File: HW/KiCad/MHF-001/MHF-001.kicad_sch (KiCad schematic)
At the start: 137 parts, among them J1 DE15_Socket_HighDensity_Mount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, J10 I2C, J11 POWER, J12 Reset, J13 AREF, J14 XTAL2, J15 XTAL1, J16 AVCC, J2 Mini-DIN-6, J3 Conn_Coaxial, J4 Conn_02x32_Odd_Even, J5 USB_B_Micro, J6 02x32, J7 SPI, J8 AVR-ISP-6, J9 Serial, M3 CY7C109D-10ZXI, M5 CY7C109D-10ZXI, Q1 BC107, U1 ATMEGA2560-16AU, U10 74HC245, U11 74HC245, U12 74HC245, U13 CH340G, U14 AMS1117-5.0, U15 AMS1117-3.3, U2 74HC14, U3 74LS08, U4 74HC165, U6 74AHC373PW, U7 74HC595, U8 74HC595, U9 74HC157, Y1 16 MHz, Y2 12 MHz

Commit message: added some connectors
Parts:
- added J17: SDcard, Connector_PinHeader_2.54mm:PinHeader_1x06_P2.54mm_Vertical, symbol Connector_Generic:Conn_01x06
- added J18: RTC1, Connector_PinHeader_2.54mm:PinHeader_1x04_P2.54mm_Vertical, symbol Connector_Generic:Conn_01x04
- added J19: RTC2, Connector_PinHeader_2.54mm:PinHeader_1x06_P2.54mm_Vertical, symbol Connector_Generic:Conn_01x06
- added J20: SDcardpins, Connector_PinHeader_2.54mm:PinHeader_1x04_P2.54mm_Vertical, symbol Connector_Generic:Conn_01x04
- added J21: 5V, Connector_PinHeader_2.54mm:PinHeader_1x02_P2.54mm_Vertical, symbol Connector_Generic:Conn_02x01
- added J22: 3.3V, Connector_PinHeader_2.54mm:PinHeader_1x02_P2.54mm_Vertical, symbol Connector_Generic:Conn_02x01
- added J23: VIN 12V, Connector_BarrelJack:BarrelJack_Horizontal, symbol Connector:Barrel_Jack_Switch
- added JP1, JP2, JP3, JP4: SolderJumper_2_Bridged, Jumper:SolderJumper-2_P1.3mm_Bridged_Pad1.0x1.5mm, symbol Jumper:SolderJumper_2_Bridged
- J11: value POWER -> 5V
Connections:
- net +3.3V: now also J22.1 (Pin_1)
- net +5V: now also J10.2 (Pin_2), J11.1 (Pin_1), J11.3 (Pin_3), J11.5 (Pin_5), J7.5 (Pin_5), J17.5 (Pin_5), J18.2 (Pin_2), J19.2 (Pin_2), J21.1 (Pin_1); no longer J10.3 (Pin_3), J7.6 (Pin_6)
- net B16: now also JP92.3 (B)
- net GND: now also J10.1 (Pin_1), J7.6 (Pin_6), J17.6 (Pin_6), J18.1 (Pin_1), J19.1 (Pin_1), J21.2 (Pin_2), J22.2 (Pin_2), J23.2, J23.3; no longer J10.4 (Pin_4), J7.5 (Pin_5)
- net MISO: now also J7.4 (Pin_4), JP1.2 (B); no longer J7.1 (Pin_1)
- net MOSI: now also J7.3 (Pin_3), JP2.2 (B); no longer J7.2 (Pin_2)
- net SCK: now also J7.2 (Pin_2), JP3.2 (B); no longer J7.3 (Pin_3)
- net SCL: now also J10.4 (Pin_4), J18.4 (Pin_4), J19.4 (Pin_4); no longer J10.1 (Pin_1)
- net SDA: now also J10.3 (Pin_3), J18.3 (Pin_3), J19.3 (Pin_3); no longer J10.2 (Pin_2)
- net SS: now also J7.1 (Pin_1), JP4.2 (B); no longer J7.4 (Pin_4)
- net VIN: now also J23.1; no longer J11.1 (Pin_1), J11.3 (Pin_3), J11.5 (Pin_5)
- new net: J17.3 (Pin_3), J20.3 (Pin_3), JP2.1 (A)
- new net: J17.4 (Pin_4), J20.4 (Pin_4), JP1.1 (A)
- new net: J17.1 (Pin_1), J20.1 (Pin_1), JP4.1 (A)
- new net: J17.2 (Pin_2), J20.2 (Pin_2), JP3.1 (A)
- no-connect marks 50 -> 52
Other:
- moved on the sheet: F1, J5, R24, R25

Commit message: Final placement of parts (I hope)
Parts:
- removed J13: AREF, Connector_Wire:SolderWire-0.5sqmm_1x01_D0.9mm_OD2.1mm, symbol Connector_Generic:Conn_01x01
- removed J14: XTAL2, Connector_Wire:SolderWire-0.5sqmm_1x01_D0.9mm_OD2.1mm, symbol Connector_Generic:Conn_01x01
- removed J15: XTAL1, Connector_Wire:SolderWire-0.5sqmm_1x01_D0.9mm_OD2.1mm, symbol Connector_Generic:Conn_01x01
- removed J16: AVCC, Connector_Wire:SolderWire-0.5sqmm_1x01_D0.9mm_OD2.1mm, symbol Connector_Generic:Conn_01x01
- removed J18: RTC1, Connector_PinHeader_2.54mm:PinHeader_1x04_P2.54mm_Vertical, symbol Connector_Generic:Conn_01x04
- removed J19: RTC2, Connector_PinHeader_2.54mm:PinHeader_1x06_P2.54mm_Vertical, symbol Connector_Generic:Conn_01x06
- removed J21: 5V, Connector_PinHeader_2.54mm:PinHeader_1x02_P2.54mm_Vertical, symbol Connector_Generic:Conn_02x01
- removed J22: 3.3V, Connector_PinHeader_2.54mm:PinHeader_1x02_P2.54mm_Vertical, symbol Connector_Generic:Conn_02x01
- removed JP89, JP90, JP93: SolderJumper_2_Bridged, Jumper:SolderJumper-2_P1.3mm_Bridged_Pad1.0x1.5mm, symbol Jumper:SolderJumper_2_Bridged
- removed N4: ~, Gilhad:NetJoint, symbol PCM_Gilhad_symbols:NetJoint
- added J24: AND_B1, Connector_Wire:SolderWire-0.5sqmm_1x01_D0.9mm_OD2.1mm, symbol Connector_Generic:Conn_01x01
- added J25: AND_B2, Connector_Wire:SolderWire-0.5sqmm_1x01_D0.9mm_OD2.1mm, symbol Connector_Generic:Conn_01x01
- added J26: AND_C1, Connector_Wire:SolderWire-0.5sqmm_1x01_D0.9mm_OD2.1mm, symbol Connector_Generic:Conn_01x01
- added J27: AND_C2, Connector_Wire:SolderWire-0.5sqmm_1x01_D0.9mm_OD2.1mm, symbol Connector_Generic:Conn_01x01
- added J28: AND_D1, Connector_Wire:SolderWire-0.5sqmm_1x01_D0.9mm_OD2.1mm, symbol Connector_Generic:Conn_01x01
- added J29: AND_D2, Connector_Wire:SolderWire-0.5sqmm_1x01_D0.9mm_OD2.1mm, symbol Connector_Generic:Conn_01x01
- added J30: AND_Dx, Connector_Wire:SolderWire-0.5sqmm_1x01_D0.9mm_OD2.1mm, symbol Connector_Generic:Conn_01x01
- added J31: AND_Cx, Connector_Wire:SolderWire-0.5sqmm_1x01_D0.9mm_OD2.1mm, symbol Connector_Generic:Conn_01x01
- added J32: AND_Bx, Connector_Wire:SolderWire-0.5sqmm_1x01_D0.9mm_OD2.1mm, symbol Connector_Generic:Conn_01x01
- added J33: NOTF, Connector_Wire:SolderWire-0.5sqmm_1x01_D0.9mm_OD2.1mm, symbol Connector_Generic:Conn_01x01
- added J34: NOTE, Connector_Wire:SolderWire-0.5sqmm_1x01_D0.9mm_OD2.1mm, symbol Connector_Generic:Conn_01x01
- added J35: NOTEx, Connector_Wire:SolderWire-0.5sqmm_1x01_D0.9mm_OD2.1mm, symbol Connector_Generic:Conn_01x01
- added J36: NOTFx, Connector_Wire:SolderWire-0.5sqmm_1x01_D0.9mm_OD2.1mm, symbol Connector_Generic:Conn_01x01
- added JP10: ANDD2+, Jumper:SolderJumper-2_P1.3mm_Bridged_Pad1.0x1.5mm, symbol Jumper:SolderJumper_2_Bridged
- added JP11: NOTF, Jumper:SolderJumper-2_P1.3mm_Bridged_Pad1.0x1.5mm, symbol Jumper:SolderJumper_2_Bridged
- added JP12: NOTE, Jumper:SolderJumper-2_P1.3mm_Bridged_Pad1.0x1.5mm, symbol Jumper:SolderJumper_2_Bridged
- added JP5: ANDB1+, Jumper:SolderJumper-2_P1.3mm_Bridged_Pad1.0x1.5mm, symbol Jumper:SolderJumper_2_Bridged
- added JP6: ANDB2+, Jumper:SolderJumper-2_P1.3mm_Bridged_Pad1.0x1.5mm, symbol Jumper:SolderJumper_2_Bridged
- added JP7: ANDC1+, Jumper:SolderJumper-2_P1.3mm_Bridged_Pad1.0x1.5mm, symbol Jumper:SolderJumper_2_Bridged
- added JP8: ANDC2+, Jumper:SolderJumper-2_P1.3mm_Bridged_Pad1.0x1.5mm, symbol Jumper:SolderJumper_2_Bridged
- added JP9: ANDD1+, Jumper:SolderJumper-2_P1.3mm_Bridged_Pad1.0x1.5mm, symbol Jumper:SolderJumper_2_Bridged
- added N1: ~, NetTie:NetTie-2_SMD_Pad0.5mm, symbol Device:NetTie_2
- C1: value 100 pF?? -> 100 pF
- J1: value DE15_Socket_HighDensity_MountingHoles -> VGA
- J11: value 5V -> + 5V -; footprint Connector_PinHeader_2.54mm:PinHeader_2x03_P2.54mm_Vertical -> Connector_PinSocket_2.54mm:PinSocket_2x03_P2.54mm_Vertical
- J2: value Mini-DIN-6 -> PS/2
- J3: value Conn_Coaxial -> RCA; footprint other.pretty:CUI_RCJ-047 -> Gilhad:CUI_RCJ-047_Yellow
- J4: value Conn_02x32_Odd_Even -> SysBus
- J5: value USB_B_Micro -> Micro
- J6: value 02x32 -> SysBus
- J8: value AVR-ISP-6 -> ISP
- JP1: value SolderJumper_2_Bridged -> MISO
- JP100: value SolderJumper_3_Open -> SHRequest
- JP102: value SolderJumper_3_Open -> S_Enable
- JP103: value SolderJumper_3_Open -> S_Read
- JP104: value SolderJumper_3_Open -> S_Write
- JP105: value SolderJumper_3_Open -> GDdir
- JP106: value SolderJumper_3_Open -> GEnable
- JP107: value SolderJumper_3_Open -> GADir
- JP2: value SolderJumper_2_Bridged -> MOSI
- JP3: value SolderJumper_2_Bridged -> SCK
- JP4: value SolderJumper_2_Bridged -> SS
- JP55: value SolderJumper_2_Bridged -> PS2_Data; footprint Jumper:SolderJumper-2_P1.3mm_Bridged_Pad1.0x1.5mm -> Jumper:SolderJumper-2_P1.3mm_Open_RoundedPad1.0x1.5mm; symbol Jumper:SolderJumper_2_Bridged -> Jumper:SolderJumper_2_Open
- JP56: value SolderJumper_2_Bridged -> PS2_CLK; footprint Jumper:SolderJumper-2_P1.3mm_Bridged_Pad1.0x1.5mm -> Jumper:SolderJumper-2_P1.3mm_Open_RoundedPad1.0x1.5mm; symbol Jumper:SolderJumper_2_Bridged -> Jumper:SolderJumper_2_Open
- JP91: value SolderJumper_2_Bridged -> Inside
- JP92: value SolderJumper_3_Open -> X16
- JP94: value SolderJumper_3_Open -> A_HALT
- JP95: value SolderJumper_3_Open -> A_READ
- JP98: value SolderJumper_3_Open -> SHDirty
- JP99: value SolderJumper_3_Open -> SHGranted
- LED1: value LED -> RX
- LED2: value LED -> TX
- LED3: value LED -> ON
- LED4: value LED -> CTS
- LED5: value LED -> RTS
- LED6: value LED -> SCL
- N3: footprint Gilhad:NetJoint -> NetTie:NetTie-2_SMD_Pad0.5mm; symbol PCM_Gilhad_symbols:NetJoint -> Device:NetTie_2
- PA1: value Conn_01x08 -> PA
- PB1: value Conn_01x08 -> PB
- PC1: value Conn_01x08 -> PC
- PD1: value Conn_01x08 -> PD
- PE1: value Conn_01x08 -> PE
- PF1: value Conn_01x08 -> PF
- PG1: value Conn_01x06 -> PG
- PH1: value Conn_01x08 -> PH
- PJ1: value Conn_01x08 -> PJ
- PK1: value Conn_01x08 -> PK
- PL1: value Conn_01x08 -> PL
- R1: value 3k3 -> 3k3/22k
- R32, R33: value --- -> 4k7; now fitted
- S1: value TS06-667-30-BK-100-G-SMT-TR -> Reset
- U1: value ATMEGA2560-16AU -> ATMEGA2560
- U6: value 74AHC373PW -> 74AHC373
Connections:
- net Data is gone; now on net PS2 Data: J2.1, R12.1, U7.14 (SER)
- net +5V: now also U1.100 (AVCC), JP10.1 (A), JP11.1 (A), JP12.1 (A), JP5.1 (A), JP6.1 (A), JP7.1 (A), JP8.1 (A), JP9.1 (A)
- net GND: no longer U2.13, U3.12, U3.13
- net PS2 Clock: now also D1.1 (K), R1.2, U2.4, U7.12 (RCLK), U8.12 (RCLK)
- net SYNC_RCA: now also N1.1
- net VGA data 3: now also N3.2; no longer N3.1
- net VGA data 4: now also N1.2
- net ~{SUPRESS}: now also N3.1; no longer N3.2
- net at U3.6: now also J32.1 (Pin_1)
- net at U2.10: now also J35.1 (Pin_1)
- net at U2.12: now also J36.1 (Pin_1); no longer U2.11
- net Clock: no longer names the net of J2.5, R13.1, U2.1
- new net: J27.1 (Pin_1), JP8.2 (B), U3.10
- new net: J31.1 (Pin_1), U3.8
- new net: J26.1 (Pin_1), JP7.2 (B), U3.9
- new net: J24.1 (Pin_1), JP5.2 (B), U3.4
- new net: J25.1 (Pin_1), JP6.2 (B), U3.5
- new net: J33.1 (Pin_1), JP11.2 (B), U2.13
- new net: J28.1 (Pin_1), JP9.2 (B), U3.12
- new net: J29.1 (Pin_1), JP10.2 (B), U3.13
- new net: J30.1 (Pin_1), U3.11
- new net: J34.1 (Pin_1), JP12.2 (B), U2.11
- no-connect marks 52 -> 48
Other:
- note added: "Clock"
- note added: "Data"
- moved on the sheet: U2E, U2F, U3B, U3D

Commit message: WayWayWay and other final touches
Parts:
- added J13: +5V, Connector_Wire:SolderWire-0.5sqmm_1x01_D0.9mm_OD2.1mm, symbol Connector_Generic:Conn_01x01
- added J14: GND, Connector_Wire:SolderWire-0.5sqmm_1x01_D0.9mm_OD2.1mm, symbol Connector_Generic:Conn_01x01
- added JP13: Xhalt, Jumper:SolderJumper-2_P1.3mm_Bridged_Pad1.0x1.5mm, symbol Jumper:SolderJumper_2_Bridged
- added LED7: SPI, LED_SMD:LED_0805_2012Metric, symbol Device:LED
- added LED8: HALT, LED_SMD:LED_0805_2012Metric, symbol Device:LED
- added R41, R43: 1k, Resistor_SMD:R_0805_2012Metric_Pad1.20x1.40mm_HandSolder, symbol Device:R
- added R42: 1k, Resistor_SMD:R_0603_1608Metric_Pad0.98x0.95mm_HandSolder, symbol Device:R
- JP12: value NOTE -> HaltLED
- PA1: value PA -> PA0
- PB1: value PB -> PB0
- PC1: value PC -> PC0
- PD1: value PD -> PD0
- PE1: value PE -> PE0
- PF1: value PF -> PF0
- PG1: value PG -> PG0
- PH1: value PH -> PH0
- PJ1: value PJ -> PJ0
- PK1: value PK -> PK0
- PL1: value PL -> PL0
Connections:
- net +5V: now also J13.1 (Pin_1), R42.1; no longer JP12.1 (A)
- net GND: now also J14.1 (Pin_1), LED7.1 (K), LED8.1 (K)
- net SCK: now also R41.2
- net X_HALT: now also JP13.2 (B), R42.2; no longer PE1.6 (Pin_6), U1.7 ((OC3C/INT5)PE5)
- net at J35.1 (Pin_1), U2.10: now also R43.2
- new net: LED8.2 (A), R43.1
- new net: JP12.1 (A), JP13.1 (A), PE1.6 (Pin_6), U1.7 ((OC3C/INT5)PE5)
- new net: LED7.2 (A), R41.1
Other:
- moved on the sheet: C12, D2, J12, R26, S1, U2E

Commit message: condensators
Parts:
- added Cx1, Cx10, Cx11, Cx12, Cx13, Cx2, Cx3, Cx4, Cx5, Cx6, Cx7, Cx8, Cx9: Cx, Capacitor_THT:C_Disc_D3.0mm_W2.0mm_P2.50mm, symbol Device:C
- added Cx14, Cx15: Cx, Capacitor_THT:CP_Radial_D5.0mm_P2.50mm, symbol Device:C_Polarized
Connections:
- net +5V: now also Cx1.1, Cx10.1, Cx11.1, Cx12.1, Cx13.1, Cx14.1, Cx15.1, Cx2.1, Cx3.1, Cx4.1, Cx5.1, Cx6.1, Cx7.1, Cx8.1, Cx9.1
- net GND: now also Cx1.2, Cx10.2, Cx11.2, Cx12.2, Cx13.2, Cx14.2, Cx15.2, Cx2.2, Cx3.2, Cx4.2, Cx5.2, Cx6.2, Cx7.2, Cx8.2, Cx9.2

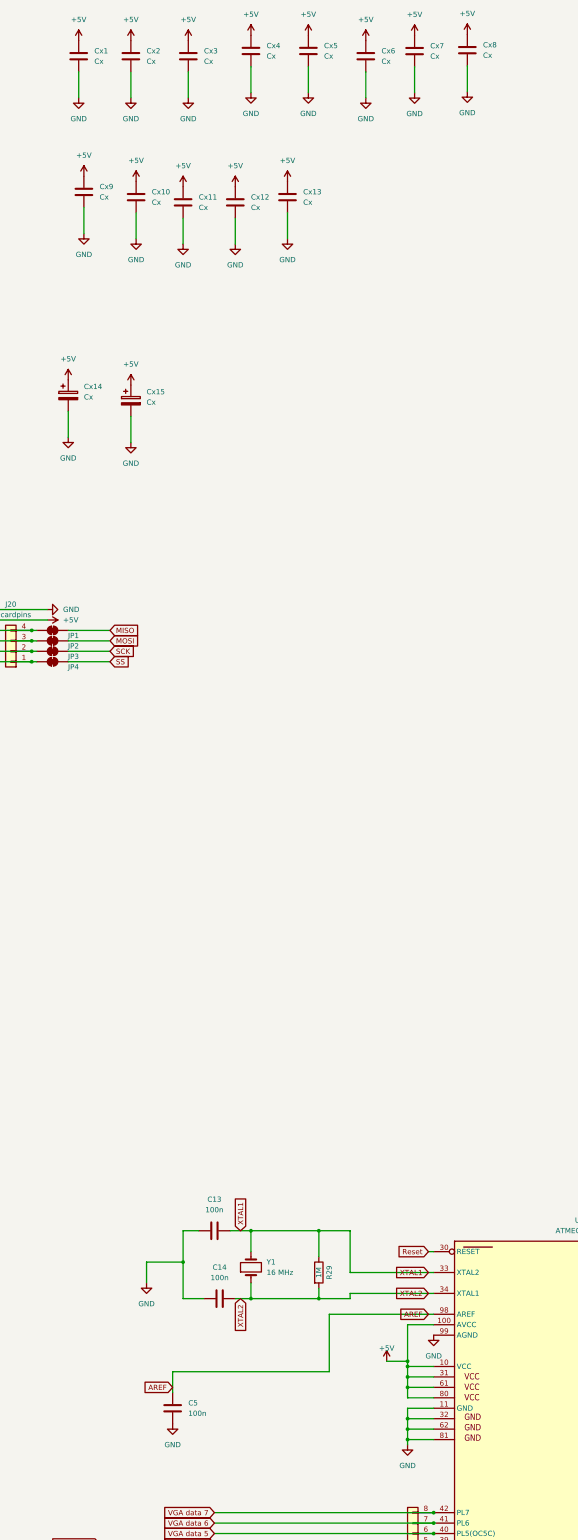
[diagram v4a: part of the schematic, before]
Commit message: XTALs, AVCC, AREF
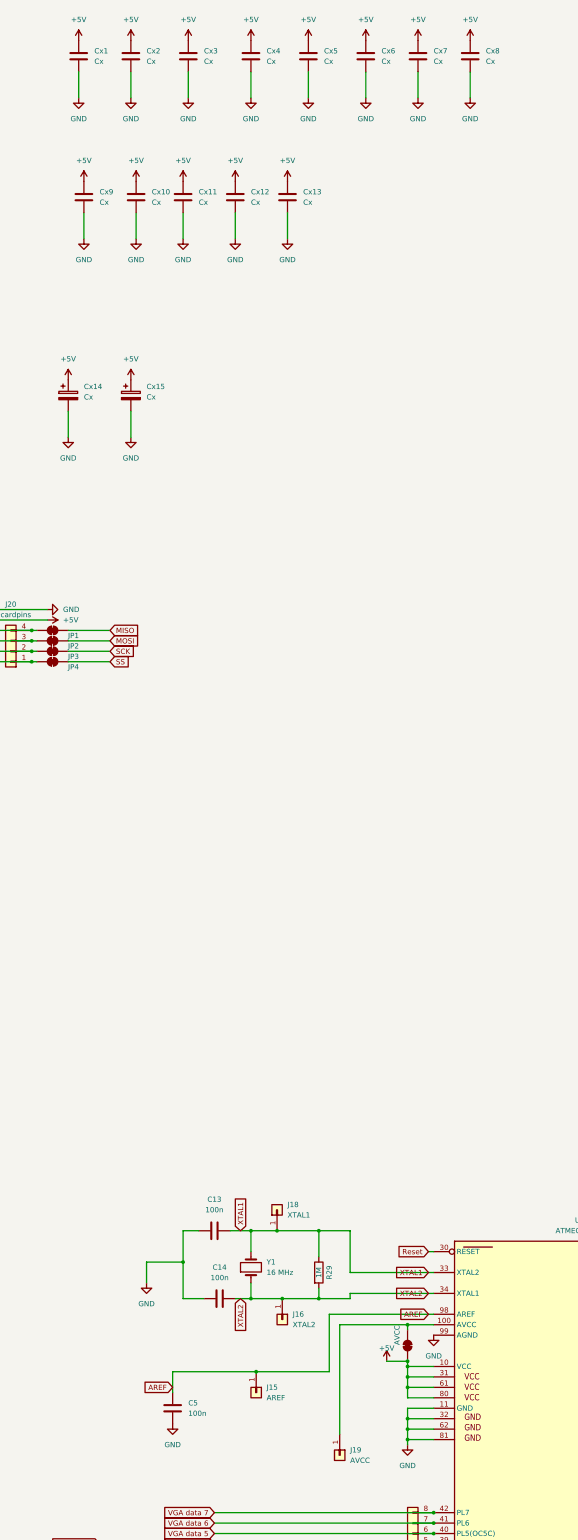
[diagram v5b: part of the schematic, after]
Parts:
- added J15: AREF, Gilhad:PinHole_1x01_2.54xrectangle, symbol PCM_Gilhad_symbols:Conn_01x01
- added J16: XTAL2, Gilhad:PinHole_1x01_2.54xrectangle, symbol PCM_Gilhad_symbols:Conn_01x01
- added J18: XTAL1, Gilhad:PinHole_1x01_2.54xrectangle, symbol PCM_Gilhad_symbols:Conn_01x01
- added J19: AVCC, Gilhad:PinHole_1x01_2.54xrectangle, symbol PCM_Gilhad_symbols:Conn_01x01
- added JP14: AVCC, Jumper:SolderJumper-2_P1.3mm_Bridged_Pad1.0x1.5mm, symbol Jumper:SolderJumper_2_Bridged
- J12, J13, J14, J24, J25, J26, J27, J28, J29, J30, J31, J32, J33, J34, J35, J36: footprint Connector_Wire:SolderWire-0.5sqmm_1x01_D0.9mm_OD2.1mm -> Gilhad:PinHole_1x01_2.54xrectangle; symbol Connector_Generic:Conn_01x01 -> PCM_Gilhad_symbols:Conn_01x01
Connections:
- net +5V: now also JP14.1 (A); no longer U1.100 (AVCC)
- net AREF: now also J15.1 (Pin_1)
- net XTAL1: now also J18.1 (Pin_1)
- net XTAL2: now also J16.1 (Pin_1)
- new net: J19.1 (Pin_1), JP14.2 (B), U1.100 (AVCC)
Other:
- moved on the sheet: Cx11, Cx12, Cx15, Cx4, Cx5, Cx7, Cx8, Cx9

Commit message: Completed
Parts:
- added J100, J101, J102, J103, J104, J105, J106, J21, J22, J37, J38, J39, J40, J41, J42, J43, J44, J45, J46, J47, J48, J49, J50, J51, J52, J53, J54, J55, J56, J57, J58, J59, J60, J61, J62, J63, J64, J65, J66, J67, J68, J69, J70, J71, J72, J73, J74, J75, J76, J77, J78, J79, J80, J81, J82, J83, J84, J85, J86, J87, J88, J89, J90, J91, J92, J93, J94, J95, J96, J97, J98, J99: x, Gilhad:PinHole_1x01_2.54xrectangle, symbol PCM_Gilhad_symbols:Conn_01x01
- added J107, J109: +3V3, Gilhad:PinHole_1x01_2.54xrectangle, symbol PCM_Gilhad_symbols:Conn_01x01
- added J108, J111, J112: GND, Gilhad:PinHole_1x01_2.54xrectangle, symbol PCM_Gilhad_symbols:Conn_01x01
- added J110: +5V, Gilhad:PinHole_1x01_2.54xrectangle, symbol PCM_Gilhad_symbols:Conn_01x01
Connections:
- net +3.3V: now also J107.1 (Pin_1), J109.1 (Pin_1)
- net +5V: now also J110.1 (Pin_1)
- net GND: now also J108.1 (Pin_1), J111.1 (Pin_1), J112.1 (Pin_1)
- no-connect marks 48 -> 120
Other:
- moved on the sheet: J16, J18
